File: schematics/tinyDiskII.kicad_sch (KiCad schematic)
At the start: 52 parts, among them J1 AVR-PDI-6, J2 SD_Card, J3 USB_B_Mini, J4 APPLEII_DISK_CONNECTOR, J5 Ext, SW1 RotaryEncoder_Switch, U1 MX25R3235FM1xx0, U10 AP1117-33, U2 SN74LVC244, U3 CH340C, U4 ATxmega16A4U-A, U5 74AHCT125, U7 OLED_MULTI

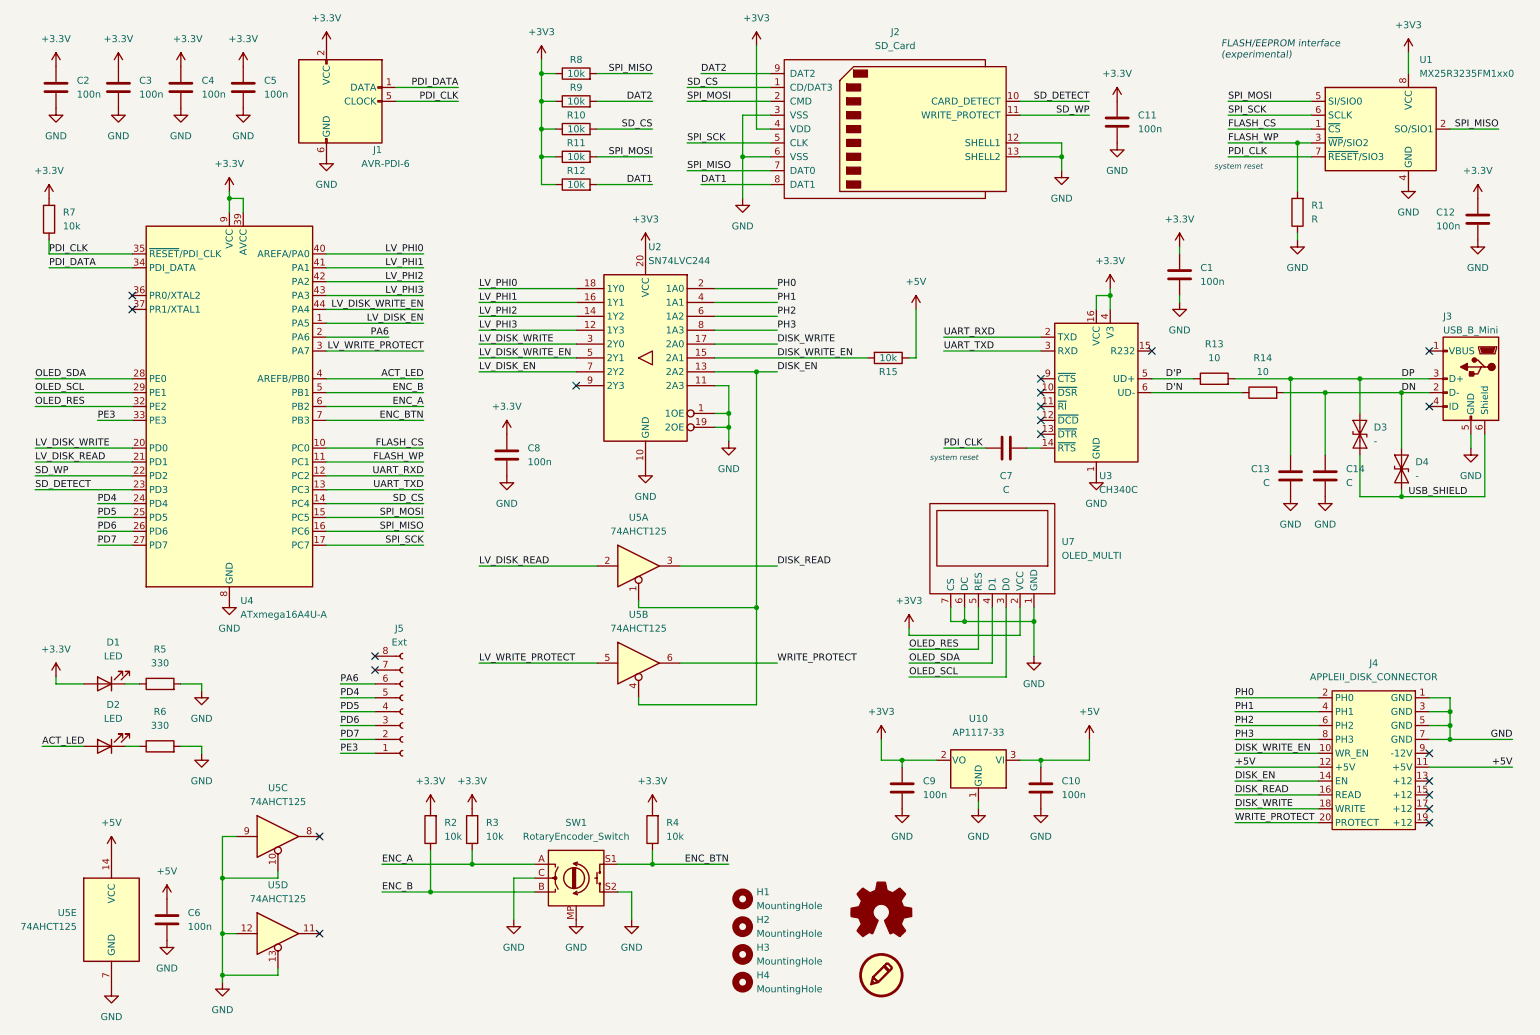
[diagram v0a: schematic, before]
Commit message: [schematics] Updated power symbols, part 2
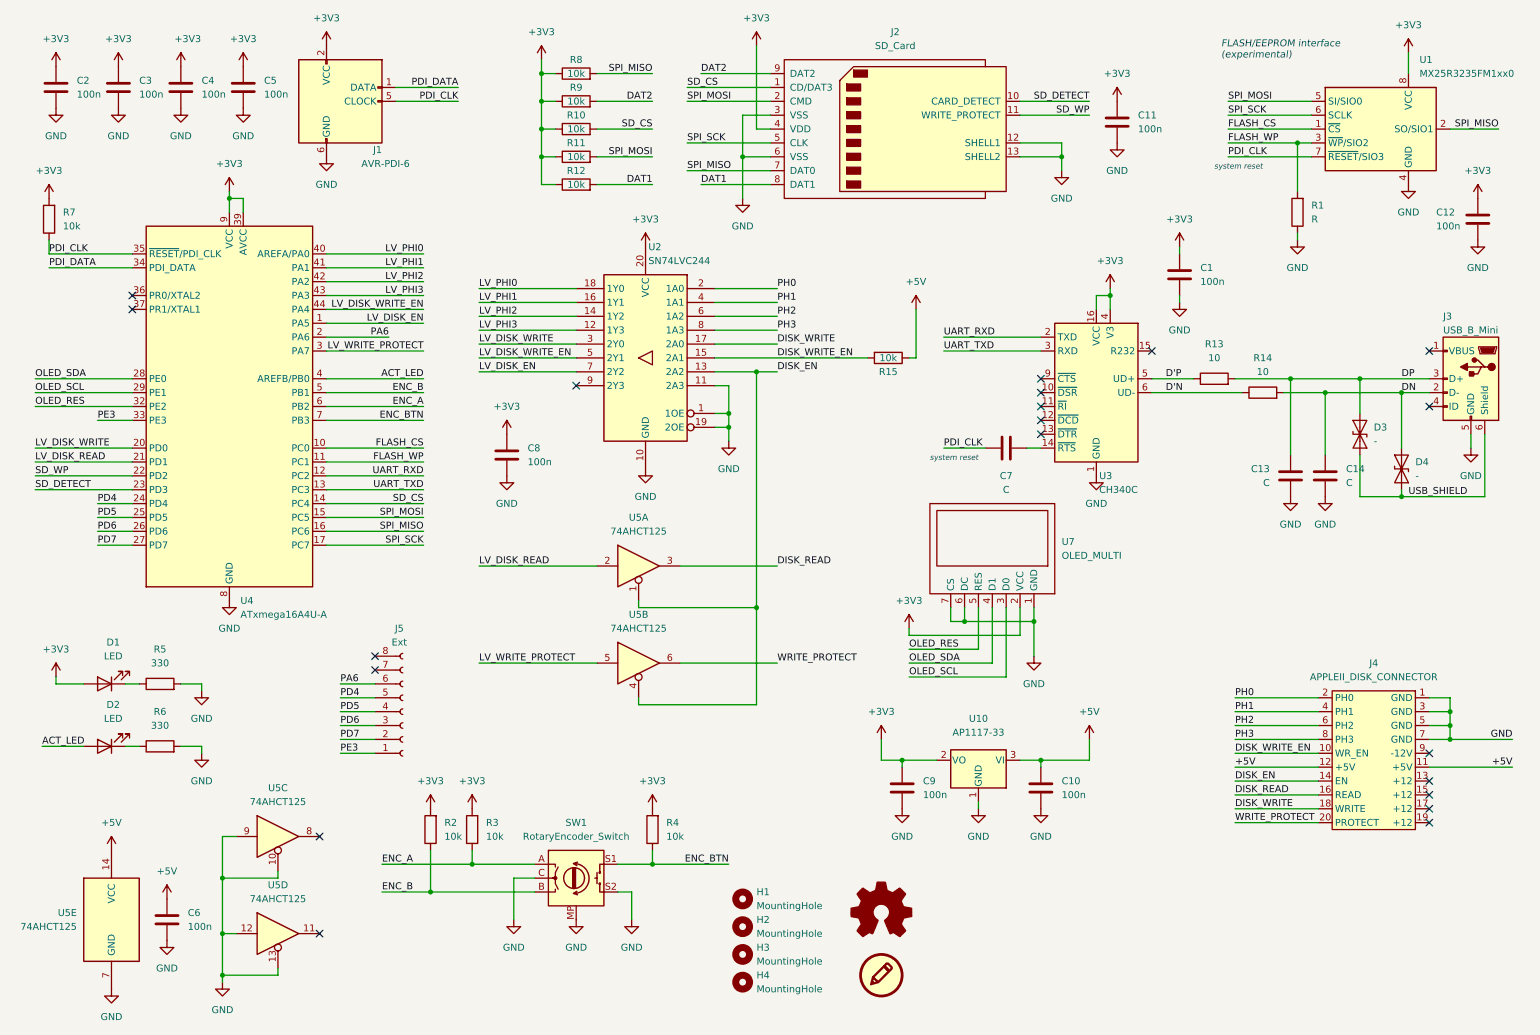
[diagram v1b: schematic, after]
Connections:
- net +3.3V is gone; now on net +3V3: C1.1, C11.1, C12.1, C2.1, C3.1, C4.1, C5.1, C8.1, D1.2 (A), J1.2 (VCC), R2.2, R3.2, R4.2, R7.2, U3.16 (VCC), U3.4 (V3), U4.19 (VCC), U4.31 (VCC), U4.39 (AVCC), U4.9 (VCC)

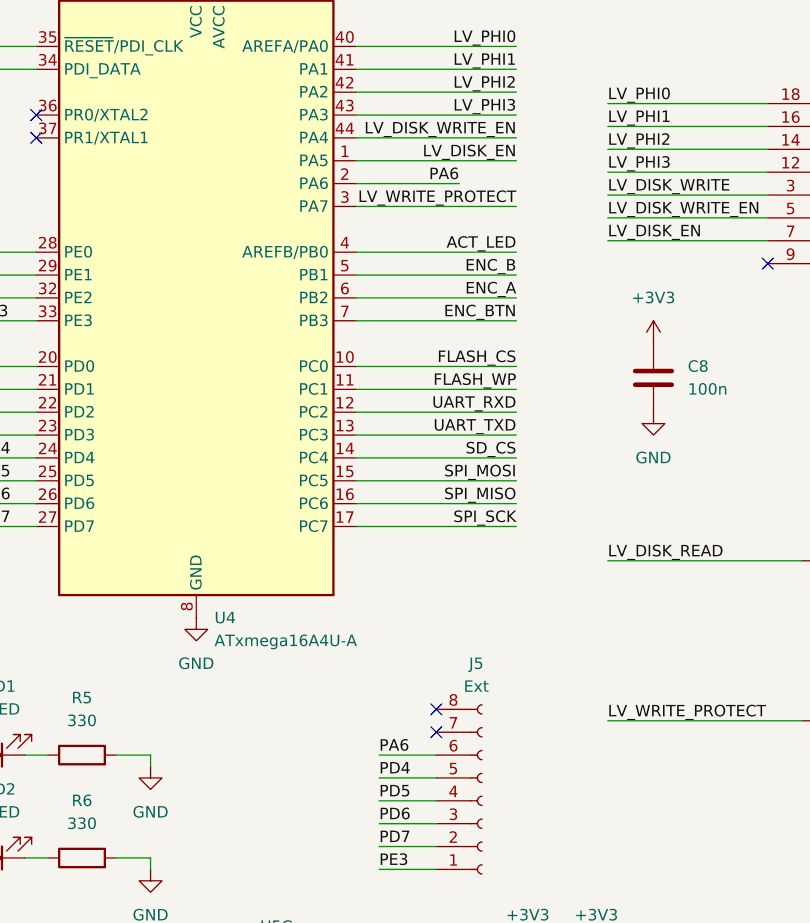
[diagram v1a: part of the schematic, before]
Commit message: [schematics] updated routing fixing errata of rev1.0
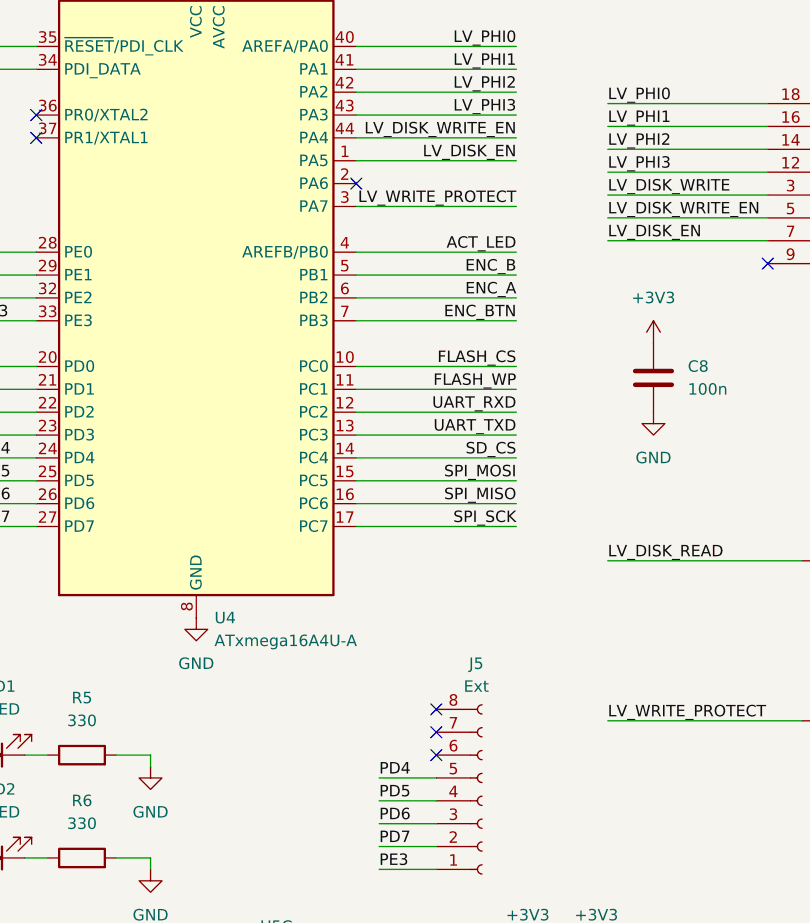
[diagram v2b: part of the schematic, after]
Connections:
- net PA6: no longer names the net of J5.6 (Pin_6)
- net PA6: no longer U4.2 (PA6)
- no-connect marks 20 -> 22
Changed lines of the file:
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@@
   (no_connect (at 113.03 81.28))
   (no_connect (at 76.2 130.81))
+  (no_connect (at 76.2 135.89))
   (no_connect (at 218.44 74.93))
   (no_connect (at 66.04 163.83))
@@
   (no_connect (at 198.12 82.55))
   (no_connect (at 198.12 80.01))
+  (no_connect (at 67.31 72.39))
   (wire (pts (xy 232.41 29.21) (xy 247.65 29.21))
     (stroke (width 0) (type default) (color 0 0 0 0))
@@
     (stroke (width 0) (type default) (color 0 0 0 0))
   )
-  (wire (pts (xy 78.74 72.39) (xy 67.31 72.39))
-    (stroke (width 0) (type default) (color 0 0 0 0))
-  )
   (wire (pts (xy 279.4 90.17) (xy 279.4 101.6))
     (stroke (width 0) (type default) (color 0 0 0 0))
@@
   )
   (wire (pts (xy 124.46 139.7) (xy 124.46 138.43))
-    (stroke (width 0) (type default) (color 0 0 0 0))
-  )
-  (wire (pts (xy 69.85 135.89) (xy 76.2 135.89))
     (stroke (width 0) (type default) (color 0 0 0 0))
   )
@@
     (effects (font (size 1.27 1.27)) (justify left bottom))
   )
-  (label "PA6" (at 69.85 135.89 0)
-    (effects (font (size 1.27 1.27)) (justify left bottom))
-  )
   (label "LV_PHI3" (at 95.25 71.12 0)
     (effects (font (size 1.27 1.27)) (justify left bottom))
@@
     (effects (font (size 1.27 1.27)) (justify left bottom))
   )
-  (label "PA6" (at 78.74 72.39 180)
-    (effects (font (size 1.27 1.27)) (justify right bottom))
-  )
   (label "PDI_DATA" (at 16.51 59.69 0)
